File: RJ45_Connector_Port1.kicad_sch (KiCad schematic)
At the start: 8 parts, among them J1 0826-1X4T-43-F

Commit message: Adding page title, and confidential for now
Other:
- title: (none) -> RJ45 Connector Port 1
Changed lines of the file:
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@@
 	(paper "A4")
 	(title_block
+		(title "RJ45 Connector Port 1")
 		(date "2025-12-21")
 		(rev "Rev. A")
 		(company "Kebag-Logic <contact@kebag-logic.com>")
+		(comment 1 "Confidential")
 	)
 	(junction

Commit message: fixes ERC errors in DC/DC converters
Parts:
- C10, C3, C8, C9: footprint Capacitor_SMD:C_0201_0603Metric -> KL_Footprints:C_0603; Dielectric X7R -> (none); Farnell 4539043 -> (none); Package_in_inch 0603 -> (none); Tolerance_in_pct 10 -> (none)
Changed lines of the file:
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@@
 		(dnp no)
 		(property "Reference" "C9"
-			(at 80.01 58.928 90)
-			(effects
-				(font
-					(size 1.27 1.27)
-				)
+			(at 77.47 61.595 0)
+			(effects
+				(font
+					(size 1.27 1.27)
+				)
+				(justify left)
 			)
 		)
 		(property "Value" "100n"
-			(at 80.01 65.532 90)
-			(effects
-				(font
-					(size 1.27 1.27)
-				)
-			)
-		)
-		(property "Footprint" "Capacitor_SMD:C_0201_0603Metric"
+			(at 82.55 61.595 0)
+			(effects
+				(font
+					(size 1.27 1.27)
+				)
+				(justify left)
+			)
+		)
+		(property "Footprint" "KL_Footprints:C_0603"
 			(at 83.82 61.2648 0)
 			(effects
@@
 		)
 		(property "LCSC" "C1591"
-			(at 80.01 62.23 0)
-			(effects
-				(font
-					(size 1.27 1.27)
-				)
-				(hide yes)
-			)
-		)
-		(property "Tolerance_in_pct" "10"
-			(at 80.01 62.23 0)
-			(effects
-				(font
-					(size 1.27 1.27)
-				)
-				(hide yes)
-			)
-		)
-		(property "Dielectric" "X7R"
-			(at 80.01 62.23 0)
-			(effects
-				(font
-					(size 1.27 1.27)
-				)
-				(hide yes)
-			)
-		)
-		(property "Package_in_inch" "0603"
-			(at 80.01 62.23 0)
-			(effects
-				(font
-					(size 1.27 1.27)
-				)
-				(hide yes)
-			)
-		)
-		(property "Farnell" "4539043"
 			(at 80.01 62.23 0)
 			(effects
@@
 		(dnp no)
 		(property "Reference" "C3"
-			(at 80.01 38.608 90)
-			(effects
-				(font
-					(size 1.27 1.27)
-				)
+			(at 77.47 41.275 0)
+			(effects
+				(font
+					(size 1.27 1.27)
+				)
+				(justify left)
 			)
 		)
 		(property "Value" "100n"
-			(at 80.01 45.212 90)
-			(effects
-				(font
-					(size 1.27 1.27)
-				)
-			)
-		)
-		(property "Footprint" "Capacitor_SMD:C_0201_0603Metric"
+			(at 82.55 41.275 0)
+			(effects
+				(font
+					(size 1.27 1.27)
+				)
+				(justify left)
+			)
+		)
+		(property "Footprint" "KL_Footprints:C_0603"
 			(at 83.82 40.9448 0)
 			(effects
@@
 		)
 		(property "LCSC" "C1591"
-			(at 80.01 41.91 0)
-			(effects
-				(font
-					(size 1.27 1.27)
-				)
-				(hide yes)
-			)
-		)
-		(property "Tolerance_in_pct" "10"
-			(at 80.01 41.91 0)
-			(effects
-				(font
-					(size 1.27 1.27)
-				)
-				(hide yes)
-			)
-		)
-		(property "Dielectric" "X7R"
-			(at 80.01 41.91 0)
-			(effects
-				(font
-					(size 1.27 1.27)
-				)
-				(hide yes)
-			)
-		)
-		(property "Package_in_inch" "0603"
-			(at 80.01 41.91 0)
-			(effects
-				(font
-					(size 1.27 1.27)
-				)
-				(hide yes)
-			)
-		)
-		(property "Farnell" "4539043"
 			(at 80.01 41.91 0)
 			(effects
@@
 		(dnp no)
 		(property "Reference" "C10"
-			(at 80.01 69.088 90)
-			(effects
-				(font
-					(size 1.27 1.27)
-				)
+			(at 77.47 71.755 0)
+			(effects
+				(font
+					(size 1.27 1.27)
+				)
+				(justify left)
 			)
 		)
 		(property "Value" "100n"
-			(at 80.01 75.692 90)
-			(effects
-				(font
-					(size 1.27 1.27)
-				)
-			)
-		)
-		(property "Footprint" "Capacitor_SMD:C_0201_0603Metric"
+			(at 82.55 71.755 0)
+			(effects
+				(font
+					(size 1.27 1.27)
+				)
+				(justify left)
+			)
+		)
+		(property "Footprint" "KL_Footprints:C_0603"
 			(at 83.82 71.4248 0)
 			(effects
@@
 		)
 		(property "LCSC" "C1591"
-			(at 80.01 72.39 0)
-			(effects
-				(font
-					(size 1.27 1.27)
-				)
-				(hide yes)
-			)
-		)
-		(property "Tolerance_in_pct" "10"
-			(at 80.01 72.39 0)
-			(effects
-				(font
-					(size 1.27 1.27)
-				)
-				(hide yes)
-			)
-		)
-		(property "Dielectric" "X7R"
-			(at 80.01 72.39 0)
-			(effects
-				(font
-					(size 1.27 1.27)
-				)
-				(hide yes)
-			)
-		)
-		(property "Package_in_inch" "0603"
-			(at 80.01 72.39 0)
-			(effects
-				(font
-					(size 1.27 1.27)
-				)
-				(hide yes)
-			)
-		)
-		(property "Farnell" "4539043"
 			(at 80.01 72.39 0)
 			(effects
@@
 		(dnp no)
 		(property "Reference" "C8"
-			(at 80.01 48.768 90)
-			(effects
-				(font
-					(size 1.27 1.27)
-				)
+			(at 77.47 51.435 0)
+			(effects
+				(font
+					(size 1.27 1.27)
+				)
+				(justify left)
 			)
 		)
 		(property "Value" "100n"
-			(at 80.01 55.372 90)
-			(effects
-				(font
-					(size 1.27 1.27)
-				)
-			)
-		)
-		(property "Footprint" "Capacitor_SMD:C_0201_0603Metric"
+			(at 82.55 51.435 0)
+			(effects
+				(font
+					(size 1.27 1.27)
+				)
+				(justify left)
+			)
+		)
+		(property "Footprint" "KL_Footprints:C_0603"
 			(at 83.82 51.1048 0)
 			(effects
@@
 			(at 80.01 52.07 0)
 			(effects
-				(font
-					(size 1.27 1.27)
-				)
-				(hide yes)
-			)
-		)
-		(property "Tolerance_in_pct" "10"
-			(at 80.01 52.07 0)
-			(effects
-				(font
-					(size 1.27 1.27)
-				)
-				(hide yes)
-			)
-		)
-		(property "Dielectric" "X7R"
-			(at 80.01 52.07 0)
-			(effects
-				(font
-					(size 1.27 1.27)
-				)
-				(hide yes)
-			)
-		)
-		(property "Package_in_inch" "0603"
-			(at 80.01 52.07 0)
-			(effects
-				(font
-					(size 1.27 1.27)
-				)
-				(hide yes)
-			)
-		)
-		(property "Farnell" "4539043"
-			(at 80.01 52.07 0)
-			(effects

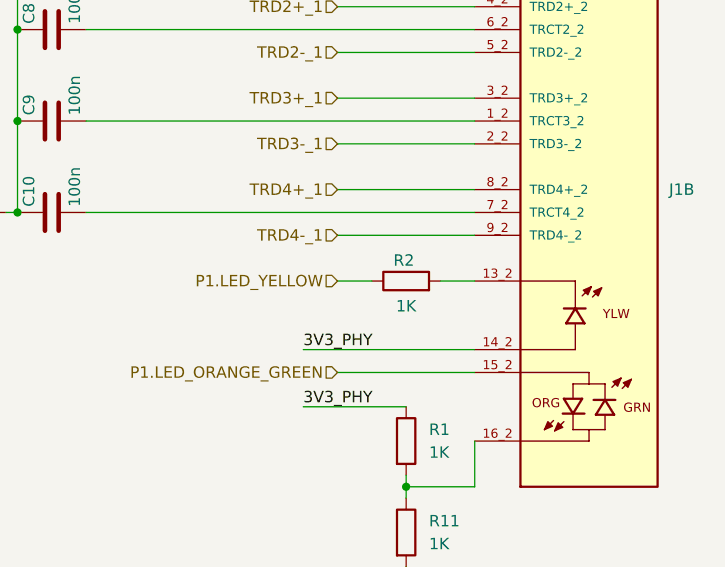
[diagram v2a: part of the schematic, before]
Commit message: updates components from my library misconfiguration. Refs: #1
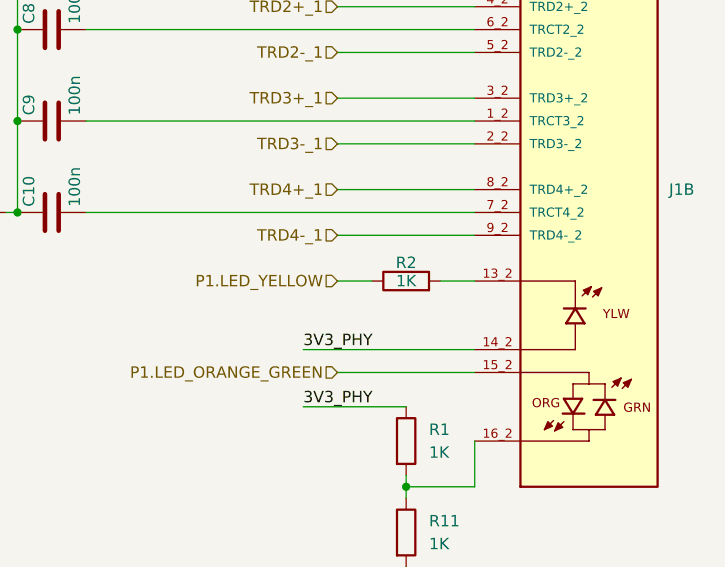
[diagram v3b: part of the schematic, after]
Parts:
- J1: footprint 0826-1X4T-43-F:BEL_0826-1X4T-43-F -> KL_Footprints:BEL_0826-1X4T-43-F
- R1, R11, R2: footprint KL_Footprints:C_0603 -> KL_Footprints:R_0603
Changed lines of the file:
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@@
 			)
 		)
-		(property "Footprint" "KL_Footprints:C_0603"
+		(property "Footprint" "KL_Footprints:R_0603"
 			(at 117.602 107.95 90)
 			(effects
@@
 			)
 		)
-		(property "Footprint" "0826-1X4T-43-F:BEL_0826-1X4T-43-F"
+		(property "Footprint" "KL_Footprints:BEL_0826-1X4T-43-F"
 			(at 139.7 69.85 0)
 			(effects
@@
 		(dnp no)
 		(property "Reference" "R2"
-			(at 119.126 77.724 90)
+			(at 119.38 77.978 90)
 			(effects
 				(font
@@
 		)
 		(property "Value" "1K"
-			(at 119.38 82.804 90)
-			(effects
-				(font
-					(size 1.27 1.27)
-				)
-			)
-		)
-		(property "Footprint" "KL_Footprints:C_0603"
+			(at 119.38 80.01 90)
+			(effects
+				(font
+					(size 1.27 1.27)
+				)
+			)
+		)
+		(property "Footprint" "KL_Footprints:R_0603"
 			(at 119.38 81.788 90)
 			(effects
@@
 			)
 		)
-		(property "Footprint" "KL_Footprints:C_0603"
+		(property "Footprint" "KL_Footprints:R_0603"
 			(at 117.602 97.79 90)
 			(effects

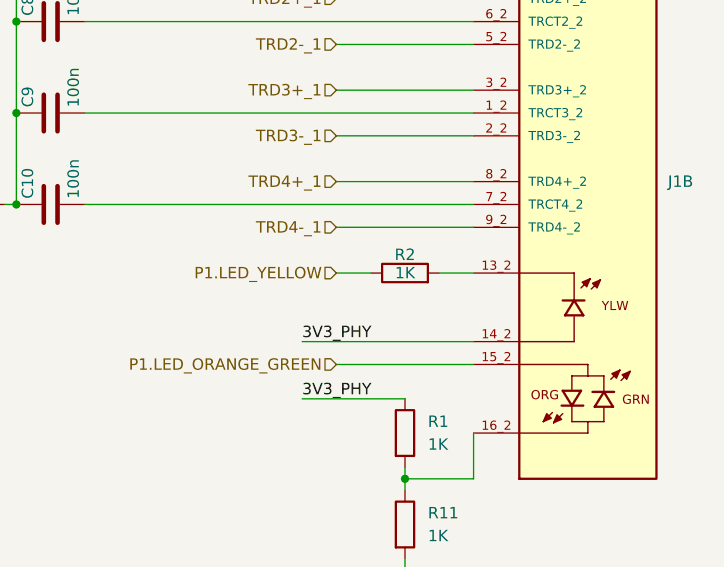
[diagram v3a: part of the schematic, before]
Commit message: removes unused busses, adds cheaper 0R resistor, clean up to fix ERC errors. Refs: #1
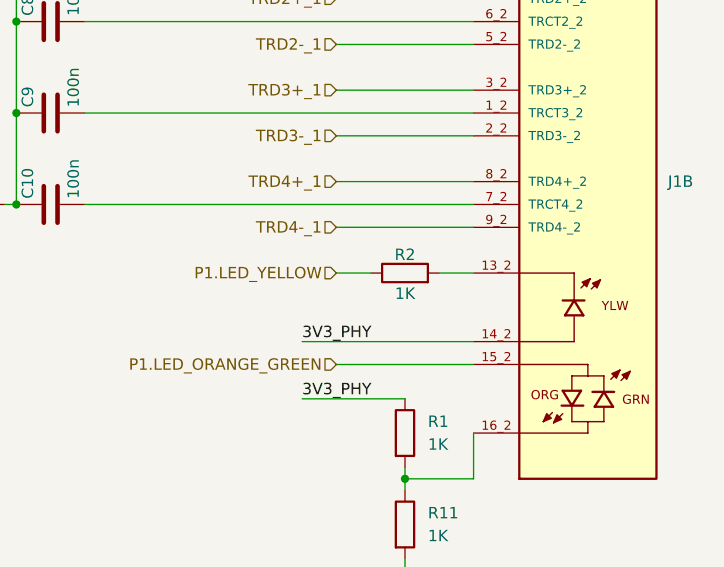
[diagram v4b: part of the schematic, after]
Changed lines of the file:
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@@
 		)
 		(property "Value" "1K"
-			(at 119.38 80.01 90)
+			(at 119.38 82.296 90)
 			(effects
 				(font
